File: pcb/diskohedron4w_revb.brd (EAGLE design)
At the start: 87.2 x 54.7 mm, 45 parts

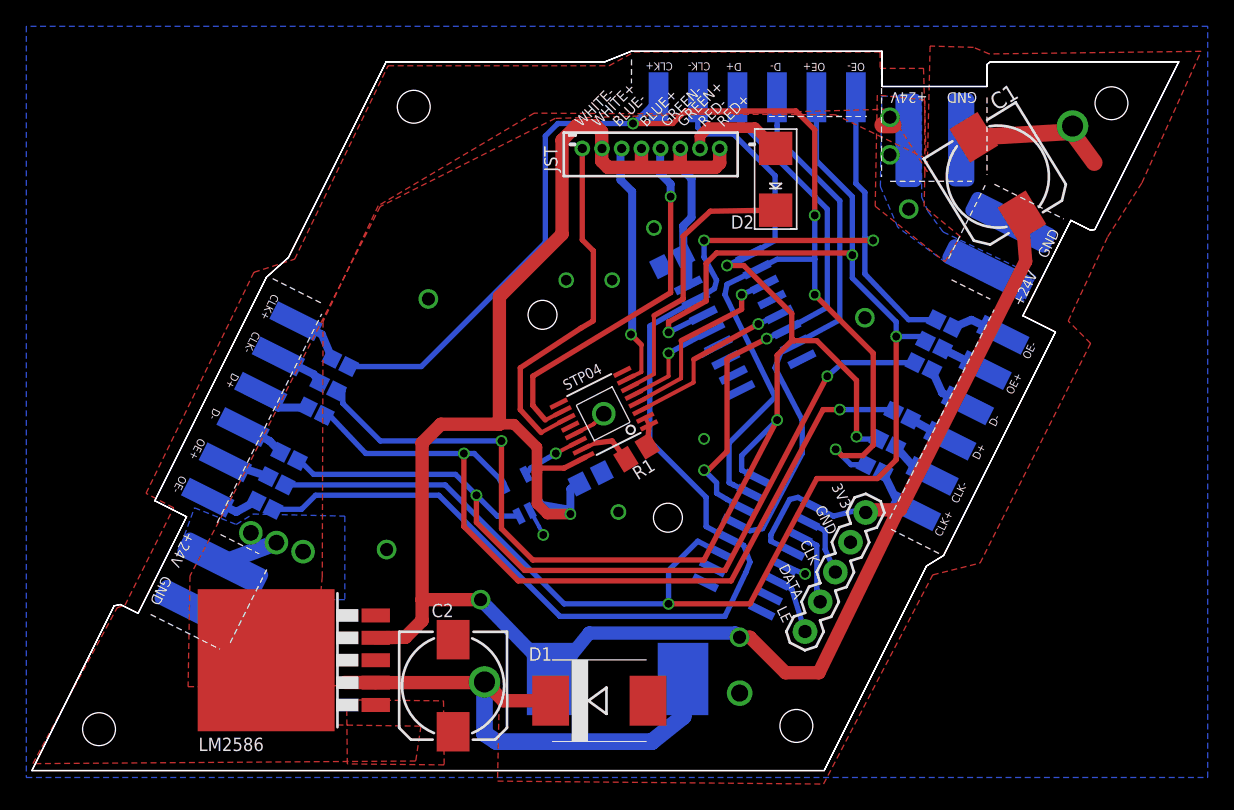
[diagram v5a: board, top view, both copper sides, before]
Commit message: order itead for rev.b and 3d trio unique model
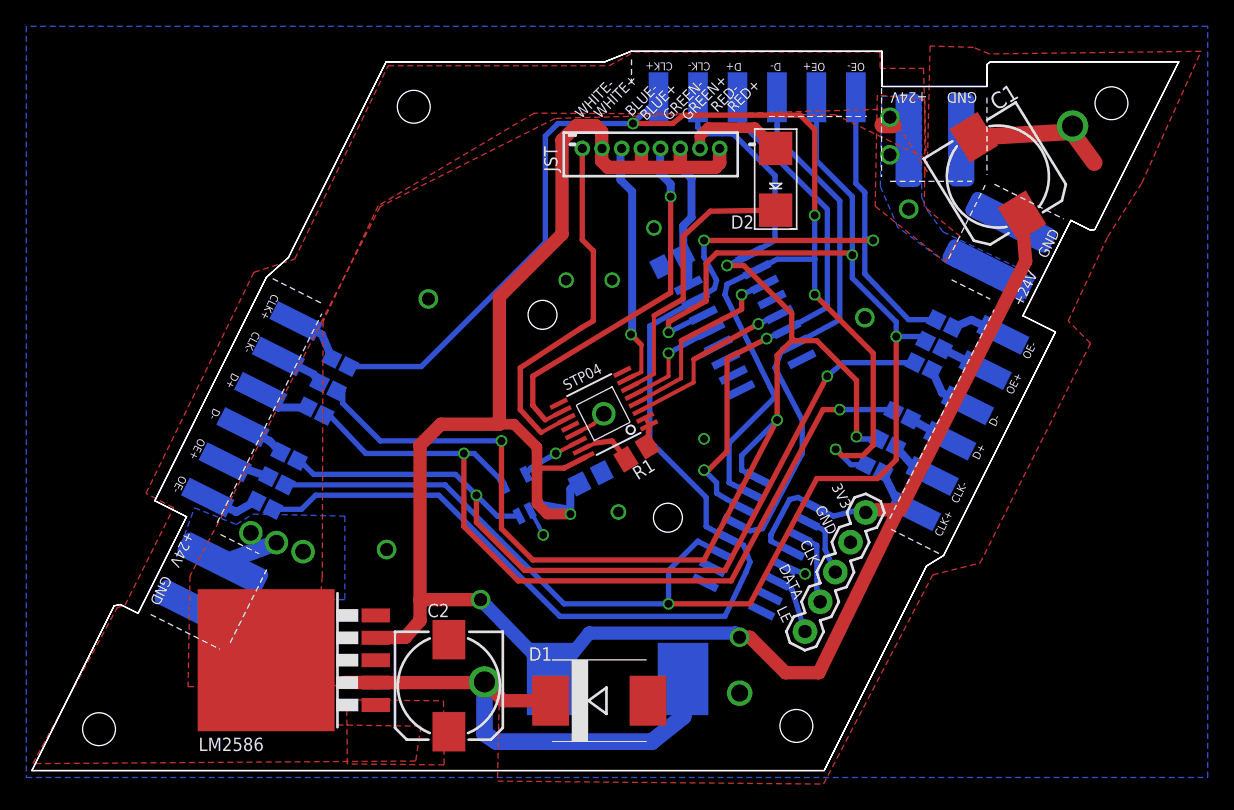
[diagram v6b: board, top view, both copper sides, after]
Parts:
- moved C2 0.32 mm to (31.7, 6.48)
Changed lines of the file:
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@@
 <grid distance="0.15875" unitdist="mm" unit="mm" style="lines" multiple="1" display="yes" altdistance="0.635" altunitdist="mm" altunit="mm"/>
 <layers>
-<layer number="1" name="Top" color="4" fill="1" visible="no" active="yes"/>
+<layer number="1" name="Top" color="4" fill="1" visible="yes" active="yes"/>
 <layer number="16" name="Bottom" color="1" fill="1" visible="yes" active="yes"/>
 <layer number="17" name="Pads" color="2" fill="1" visible="yes" active="yes"/>
 <layer number="18" name="Vias" color="2" fill="1" visible="yes" active="yes"/>
 <layer number="19" name="Unrouted" color="6" fill="1" visible="yes" active="yes"/>
-<layer number="20" name="Dimension" color="15" fill="1" visible="no" active="yes"/>
-<layer number="21" name="tPlace" color="7" fill="1" visible="no" active="yes"/>
+<layer number="20" name="Dimension" color="15" fill="1" visible="yes" active="yes"/>
+<layer number="21" name="tPlace" color="7" fill="1" visible="yes" active="yes"/>
 <layer number="22" name="bPlace" color="7" fill="1" visible="no" active="yes"/>
-<layer number="23" name="tOrigins" color="15" fill="1" visible="no" active="yes"/>
+<layer number="23" name="tOrigins" color="15" fill="1" visible="yes" active="yes"/>
 <layer number="24" name="bOrigins" color="15" fill="1" visible="no" active="yes"/>
-<layer number="25" name="tNames" color="7" fill="1" visible="no" active="yes"/>
+<layer number="25" name="tNames" color="7" fill="1" visible="yes" active="yes"/>
 <layer number="26" name="bNames" color="7" fill="1" visible="no" active="yes"/>
 <layer number="27" name="tValues" color="7" fill="1" visible="no" active="yes"/>
 <layer number="28" name="bValues" color="7" fill="1" visible="no" active="yes"/>
 <layer number="29" name="tStop" color="7" fill="3" visible="no" active="yes"/>
-<layer number="30" name="bStop" color="7" fill="6" visible="yes" active="yes"/>
+<layer number="30" name="bStop" color="7" fill="6" visible="no" active="yes"/>
 <layer number="31" name="tCream" color="7" fill="4" visible="no" active="yes"/>
-<layer number="32" name="bCream" color="7" fill="5" visible="yes" active="yes"/>
+<layer number="32" name="bCream" color="7" fill="5" visible="no" active="yes"/>
 <layer number="33" name="tFinish" color="6" fill="3" visible="no" active="yes"/>
 <layer number="34" name="bFinish" color="6" fill="6" visible="no" active="yes"/>
@@
 <layer number="250" name="Descript" color="7" fill="1" visible="no" active="yes"/>
 <layer number="251" name="SMDround" color="7" fill="1" visible="no" active="yes"/>
-<layer number="253" name="geo_helper_axis" color="14" fill="1" visible="no" active="yes"/>
+<layer number="253" name="geo_helper_axis" color="14" fill="1" visible="yes" active="yes"/>
 <layer number="254" name="cooling" color="7" fill="1" visible="no" active="yes"/>
 <layer number="255" name="geo-helper" color="13" fill="1" visible="no" active="yes"/>
@@
 <text x="62.373278125" y="20.2160125" size="0.8128" layer="25" font="vector" rot="R116.4">3V3</text>
 <text x="19.224978125" y="15.206425" size="1.016" layer="115" font="vector" rot="MR296.4">+24V</text>
-<text x="41.788390625" y="48.9012125" size="0.8128" layer="25" font="vector" rot="R45">WHITE-</text>
+<text x="41.788390625" y="49.5362125" size="0.8128" layer="25" font="vector" rot="R45">WHITE-</text>
 <wire x1="21.972484375" y1="35.54919375" x2="22.332365625" y2="35.370740625" width="0.1" layer="115"/>
 <wire x1="22.332365625" y1="35.370740625" x2="22.077909375" y2="34.87209375" width="0.1" layer="115"/>
@@
 <wire x1="73.18734375" y1="44.59560625" x2="78.462853125" y2="41.953828125" width="0.1" layer="25" style="shortdash"/>
 <text x="40.64" y="28.8925" size="0.8128" layer="25" rot="SR26.6">STP04</text>
-<text x="43.058390625" y="48.9012125" size="0.8128" layer="25" font="vector" rot="R45">WHITE+</text>
-<text x="44.645890625" y="48.9012125" size="0.8128" layer="25" font="vector" rot="R45">BLUE-</text>
-<text x="46.709640625" y="48.9012125" size="0.8128" layer="25" font="vector" rot="R45">BLUE+</text>
-<text x="48.297140625" y="48.9012125" size="0.8128" layer="25" font="vector" rot="R45">GREEN-</text>
-<text x="49.567140625" y="48.9012125" size="0.8128" layer="25" font="vector" rot="R45">GREEN+</text>
-<text x="51.154640625" y="48.9012125" size="0.8128" layer="25" font="vector" rot="R45">RED-</text>
-<text x="52.583390625" y="48.9012125" size="0.8128" layer="25" font="vector" rot="R45">RED+</text>
+<text x="43.217140625" y="49.5362125" size="0.8128" layer="25" font="vector" rot="R45">WHITE+</text>
+<text x="45.598390625" y="49.6949625" size="0.8128" layer="25" font="vector" rot="R45">BLUE-</text>
+<text x="46.709640625" y="49.3774625" size="0.8128" layer="25" font="vector" rot="R45">BLUE+</text>
+<text x="48.455890625" y="49.3774625" size="0.8128" layer="25" font="vector" rot="R45">GREEN-</text>
+<text x="49.884640625" y="49.3774625" size="0.8128" layer="25" font="vector" rot="R45">GREEN+</text>
+<text x="52.107140625" y="50.0124625" size="0.8128" layer="25" font="vector" rot="R45">RED-</text>
+<text x="53.377140625" y="50.0124625" size="0.8128" layer="25" font="vector" rot="R45">RED+</text>
 <text x="13.845478125" y="27.620090625" size="0.6096" layer="25" rot="SR243.4">D-</text>
 <text x="15.26475625" y="30.303796875" size="0.6096" layer="25" rot="SR243.4">D+</text>
@@
 <attribute name="NAME" x="73.34514375" y="50.135646875" size="1.27" layer="25" rot="R31.5"/>
 </element>
-<element name="C2" library="rcl" package="175TMP-0810" value="220uF" x="32.04029375" y="6.47505" smashed="yes" rot="R270">
-<attribute name="NAME" x="30.40483125" y="11.684659375" size="1.016" layer="25"/>
+<element name="C2" library="rcl" package="175TMP-0810" value="220uF" x="31.72279375" y="6.47505" smashed="yes" rot="R270">
+<attribute name="NAME" x="30.08733125" y="11.684659375" size="1.016" layer="25"/>
 </element>
 <element name="1D" library="diskohedron" package="SOT23-5" value="DS90LV011A" x="37.319575" y="20.958203125" smashed="yes" rot="MR333.4"/>
@@
 <wire x1="40.3225" y1="47.9425" x2="41.43375" y2="49.05375" width="1.016" layer="1"/>
 <wire x1="35.56" y1="26.3525" x2="31.115" y2="26.3525" width="1.016" layer="1"/>
-<wire x1="31.115" y1="26.3525" x2="29.68625" y2="24.92375" width="1.016" layer="1"/>
-<wire x1="29.68625" y1="24.92375" x2="29.68625" y2="13.0175" width="1.016" layer="1"/>
-<wire x1="34.13125" y1="13.0175" x2="29.68625" y2="13.0175" width="1.016" layer="1"/>
+<wire x1="31.115" y1="26.3525" x2="29.5275" y2="24.765" width="1.016" layer="1"/>
+<wire x1="29.5275" y1="24.765" x2="29.5275" y2="13.0175" width="1.016" layer="1"/>
+<wire x1="34.13125" y1="13.0175" x2="29.5275" y2="13.0175" width="1.016" layer="1"/>
 <wire x1="49.550365625" y1="39.179459375" x2="49.53" y2="41.43375" width="0.6096" layer="16"/>
 <wire x1="49.53" y1="41.43375" x2="50.165" y2="42.06875" width="0.6096" layer="16"/>
 <wire x1="49.9262" y1="36.909925" x2="49.9262" y2="38.803625" width="0.6096" layer="16"/>
 <wire x1="49.9262" y1="38.803625" x2="49.550365625" y2="39.179459375" width="0.6096" layer="16"/>
-<wire x1="29.68625" y1="13.0175" x2="29.68625" y2="11.43" width="1.016" layer="1"/>
-<wire x1="29.68625" y1="11.43" x2="28.41625" y2="10.16" width="1.016" layer="1"/>
+<wire x1="29.5275" y1="13.0175" x2="29.5275" y2="11.43" width="1.016" layer="1"/>
+<wire x1="29.5275" y1="11.43" x2="28.41625" y2="10.16" width="1.016" layer="1"/>
 <wire x1="38.751109375" y1="20.221171875" x2="40.580078125" y2="19.903671875" width="0.6096" layer="16"/>
 <wire x1="40.580078125" y1="19.903671875" x2="40.9575" y2="19.52625" width="0.6096" layer="16"/>
@@
 <wire x1="29.627053125" y1="30.738303125" x2="39.0525" y2="40.16375" width="0.4064" layer="16"/>
 <via x="45.72" y="49.2125" extent="1-16" drill="0.6"/>
-<wire x1="58.1025" y1="50.165" x2="59.53125" y2="48.73625" width="0.4064" layer="1"/>
+<wire x1="58.42" y1="49.8475" x2="59.53125" y2="48.73625" width="0.4064" layer="1"/>
 <wire x1="46.705746875" y1="50.165" x2="45.72" y2="49.2125" width="0.4064" layer="16"/>
 <wire x1="45.72" y1="49.2125" x2="48.73625" y2="49.2125" width="0.4064" layer="1"/>
-<wire x1="48.73625" y1="49.2125" x2="49.68875" y2="50.165" width="0.4064" layer="1"/>
-<wire x1="49.68875" y1="50.165" x2="58.1025" y2="50.165" width="0.4064" layer="1"/>
+<wire x1="48.73625" y1="49.2125" x2="49.53" y2="49.8475" width="0.4064" layer="1"/>
+<wire x1="49.53" y1="49.8475" x2="58.42" y2="49.8475" width="0.4064" layer="1"/>
 <wire x1="39.0525" y1="40.16375" x2="39.0525" y2="48.26" width="0.4064" layer="16"/>
 <wire x1="39.0525" y1="48.26" x2="40.005" y2="49.2125" width="0.4064" layer="16"/>
